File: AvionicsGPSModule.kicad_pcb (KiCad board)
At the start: 4 copper layers, 60 x 56.1 mm, 32 parts, among them P1 MC311D, Q1 AO3400A, U2 AP2112K-3.3, U3 L80-R, U4 RP2040, U6 W25Q128JVS, X1 ABM8-272-T3

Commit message: Connector Changes
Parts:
- moved R4 6.17 mm to (152.4, 93.6)
- moved R5 6.15 mm to (153.4, 93.6)
- moved R2 3.28 mm to (154.3, 80.0), turned to -90 degrees
- moved C17 2.51 mm to (157.5, 93.2)
- moved C19 2.51 mm to (158.5, 92.2)
- moved C1 2.49 mm to (156.5, 94.2)
- moved R3 1.99 mm to (151.4, 80.1), turned to -90 degrees
- moved P1 1.37 mm to (153.0, 75.8), turned to 180 degrees
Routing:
- net /DN: track 17.2 -> 0.58 mm
- net /DP: track 11.4 -> 0.58 mm
- net Net-(U4-USB_DM): track 8.39 -> 1.48 mm
- net Net-(U4-USB_DP): track 7.81 -> 1.21 mm
- net GND: track 92.9 -> 96.7 mm, vias 3 -> 6
- net Net-(P1-CC1): track 3.81 -> 1.44 mm
- net +5V: track 45.1 -> 44.9 mm, vias 4 -> 2

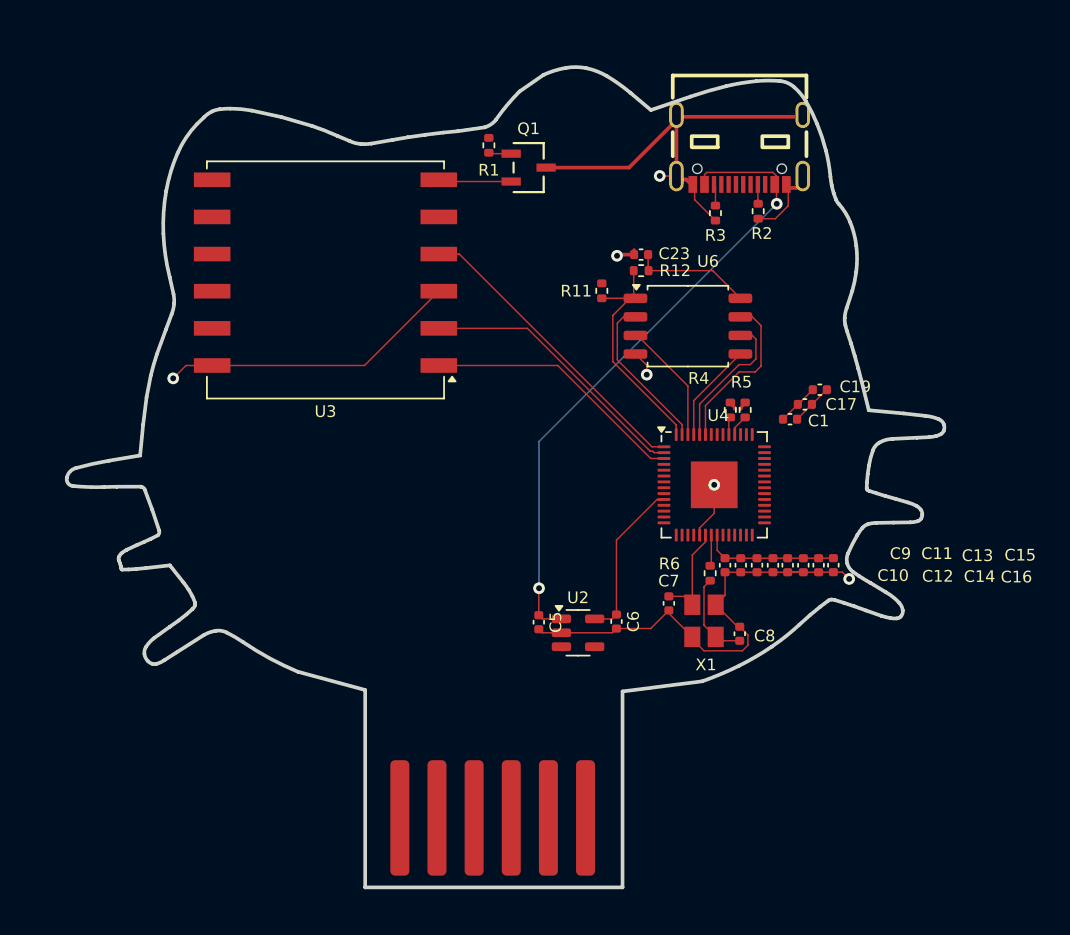
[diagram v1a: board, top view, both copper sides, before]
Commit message: Fix: Moved RP2040 capacitors
Fix: Corrected Design Rules for clearance and width

Fix: Correctly Annotated capacitors
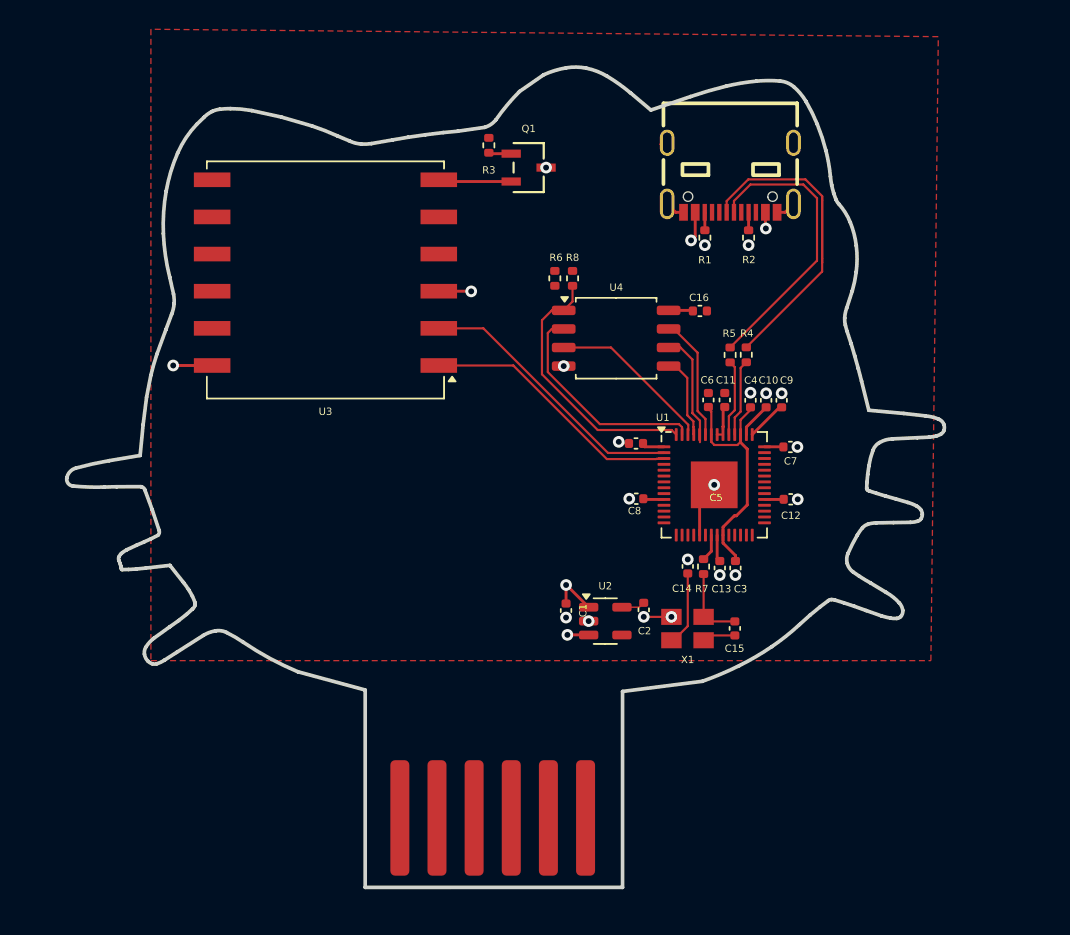
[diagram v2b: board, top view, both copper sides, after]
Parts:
- moved C3 13.5 mm to (152.8, 104.4), turned to -90 degrees
- moved C11 12.5 mm to (152.0, 92.9), turned to 90 degrees
- moved C8 11.7 mm to (145.9, 95.9), turned to 180 degrees
- moved C10 11.4 mm to (154.8, 92.9), turned to 90 degrees
- moved C9 11.3 mm to (155.9, 92.9), turned to 90 degrees
- moved C7 8.77 mm to (156.5, 96.1), turned to 0 degrees
- moved C13 7.77 mm to (151.7, 104.4)
- moved C5 7.59 mm to (146.0, 99.7), turned to 180 degrees
- moved C6 5.74 mm to (150.9, 92.9), turned to 90 degrees
- moved C16 5.57 mm to (150.3, 86.8), turned to 0 degrees
- moved U4 4.98 mm to (144.6, 88.7)
- moved C12 4.90 mm to (156.5, 99.7), turned to 0 degrees
- moved R8 4.72 mm to (141.6, 84.6), turned to -90 degrees
- moved R4 3.77 mm to (153.5, 89.8)
- moved R5 3.76 mm to (152.4, 89.8)
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- renumbered C5 to C1, C13 to C10, C14 to C11, C15 to C12, C16 to C13, C7 to C14, C8 to C15, C23 to C16, C6 to C2, C19 to C3, C17 to C4, C9 to C5, C1 to C6, C10 to C7, C11 to C8, C12 to C9, R3 to R1, R1 to R3, R5 to R4, R4 to R5, R11 to R6, R6 to R7, R12 to R8, U4 to U1, U6 to U4
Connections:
- C16 pad 1: +3V3 -> +3.3V
- R8 pad 1: +3V3 -> +3.3V
- U4 pad 8: +3V3 -> +3.3V
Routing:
- net GND: track 96.7 -> 16.9 mm, vias 6 -> 25
- net +5V: track 44.9 -> 7.89 mm, vias 2 -> 4
- net /DN: track 0.58 -> 25.4 mm
- net +3.3V: track 41.2 -> 17.5 mm
- net /DP: track 0.58 -> 20.0 mm
- net +1V1: track 2.85 -> 17.3 mm
- net +3V3: track 8.17 -> 0.00 mm
- net /QSPI_SD1: track 10.9 -> 15.1 mm
- net Net-(U1-USB_DP): track 1.21 -> 5.24 mm
- net Net-(U1-USB_DM): track 1.48 -> 5.27 mm
- net /QSPI_SD3: track 11.3 -> 7.95 mm
- net /QSPI_SD2: track 8.34 -> 11.1 mm
- net /QSPI_SS: track 16.2 -> 18.3 mm
- net /QSPI_SCLK: track 9.74 -> 7.84 mm
- net /XIN: track 6.97 -> 5.39 mm
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- added copper zone on F.Cu, net +3.3V

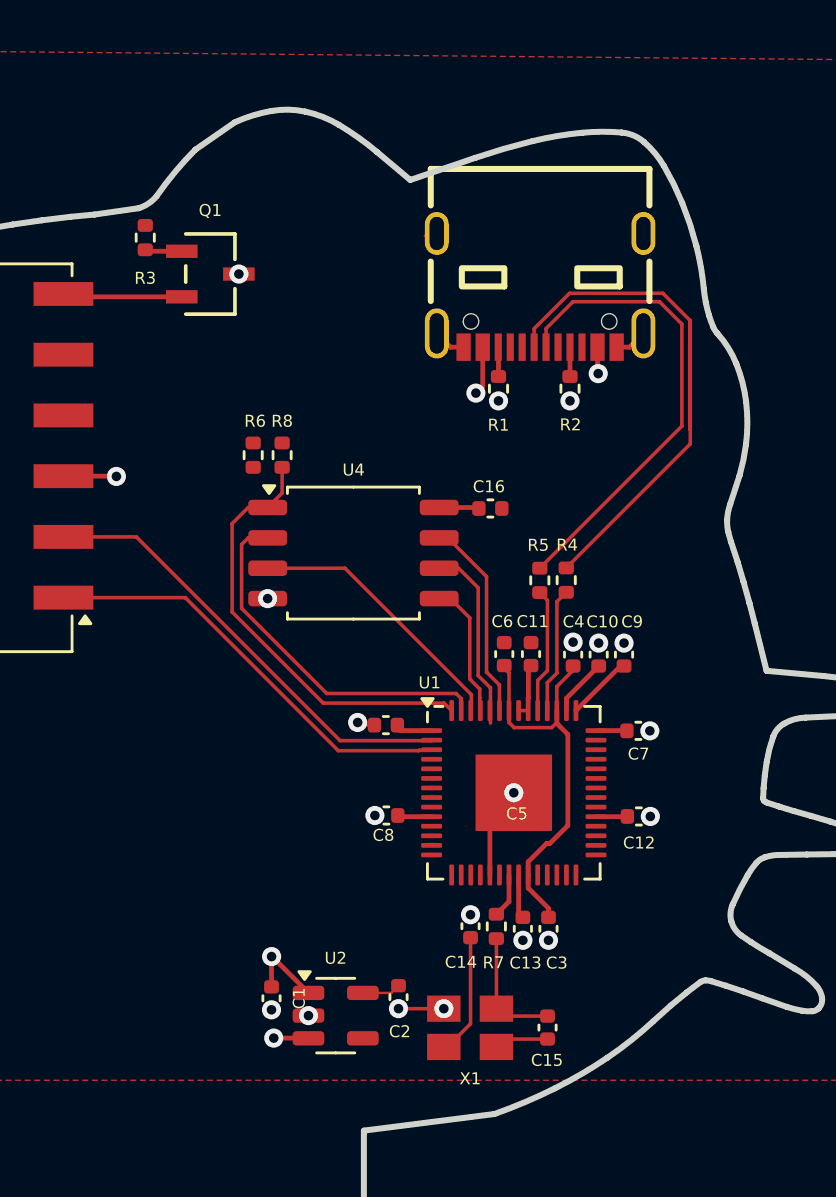
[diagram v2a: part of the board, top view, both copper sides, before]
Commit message: Fixed connector placement and GND vias
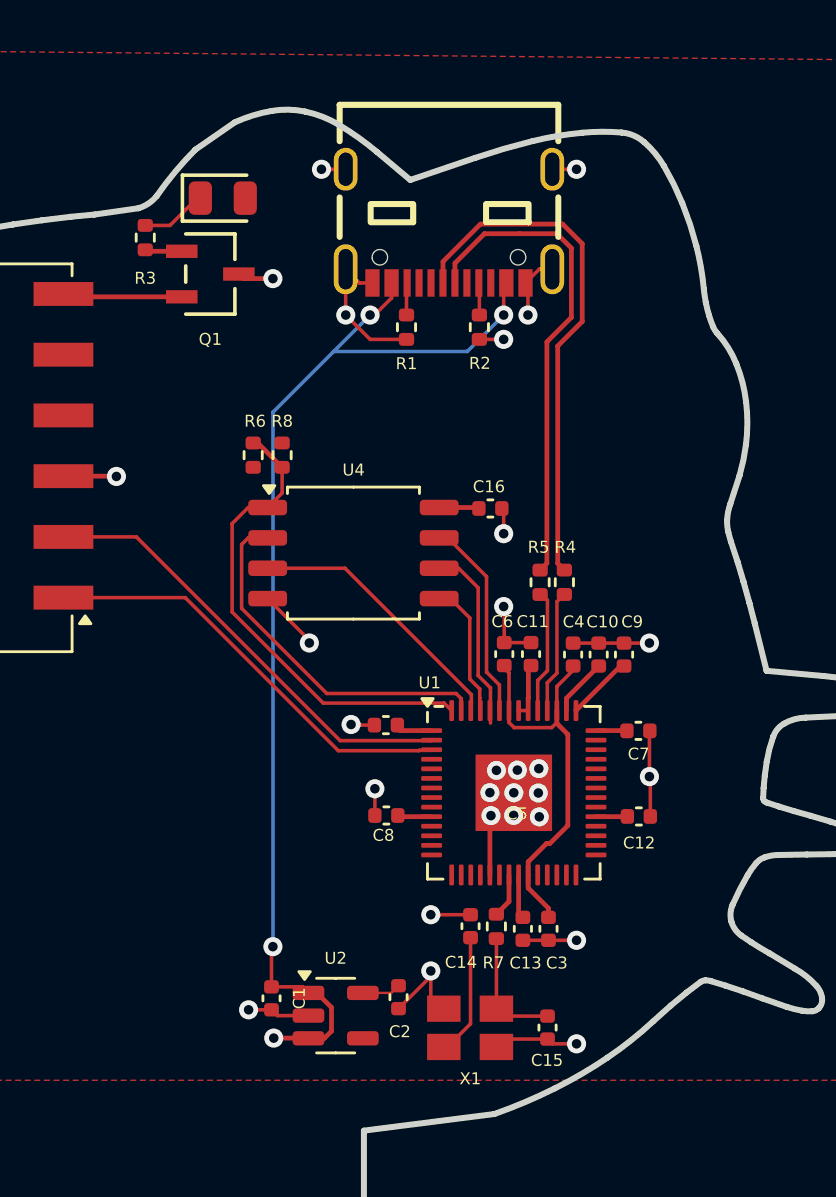
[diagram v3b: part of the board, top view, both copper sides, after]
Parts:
- added D2: Green, PCM_JLCPCB:D_0805, F.Cu at (139.1, 73.9)
- moved P1 4.66 mm to (148.6, 75.0)
- moved R1 4.63 mm to (146.8, 79.2)
- moved R2 4.58 mm to (149.9, 79.2)
- moved R4 0.12 mm to (153.4, 89.9)
- moved R5 0.08 mm to (152.4, 89.9)
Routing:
- net +5V: track 7.89 -> 47.2 mm
- net GND: track 16.9 -> 51.7 mm, vias 25 -> 29
- net /DN: track 25.4 -> 21.9 mm
- net Net-(D2-Pad1): track 0.00 -> 2.20 mm
- net /QSPI_SS: track 18.3 -> 19.9 mm

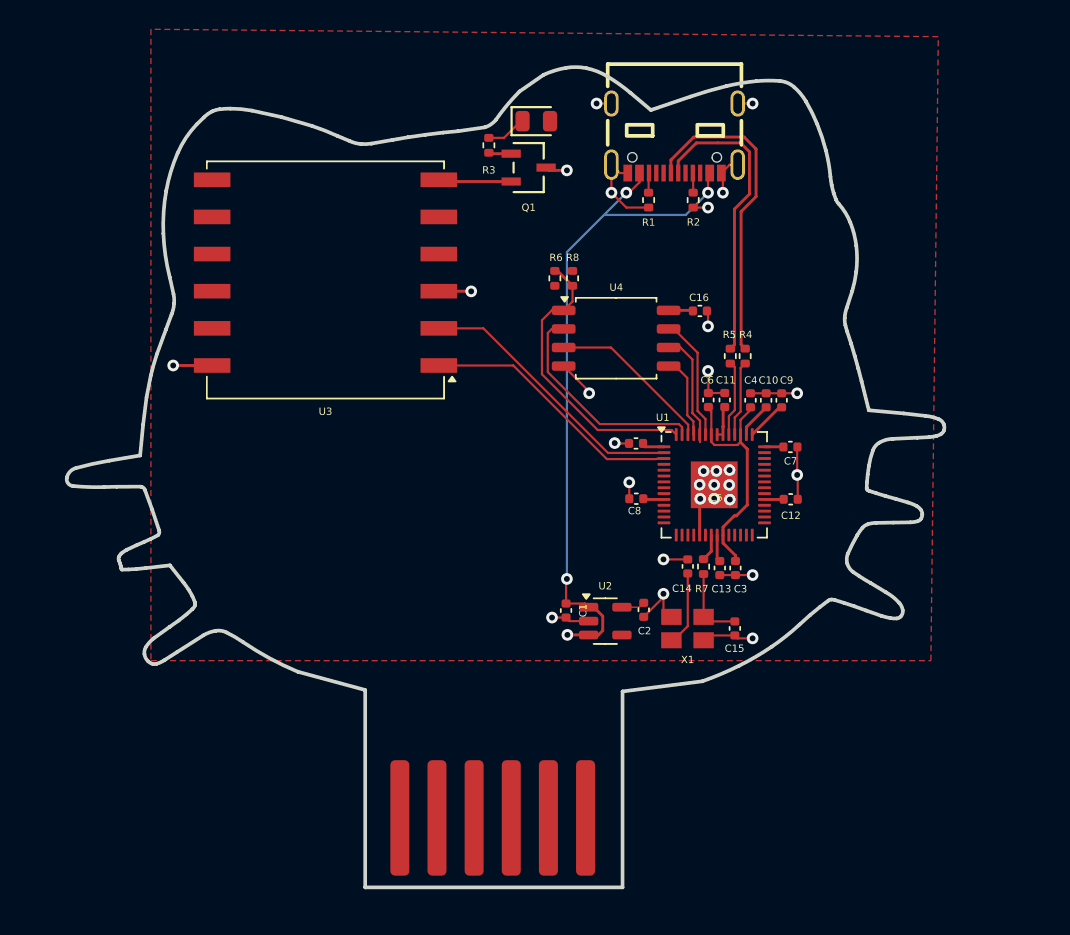
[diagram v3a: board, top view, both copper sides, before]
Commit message: Added JLC DRC requirements, and managed libraries for simpler forking
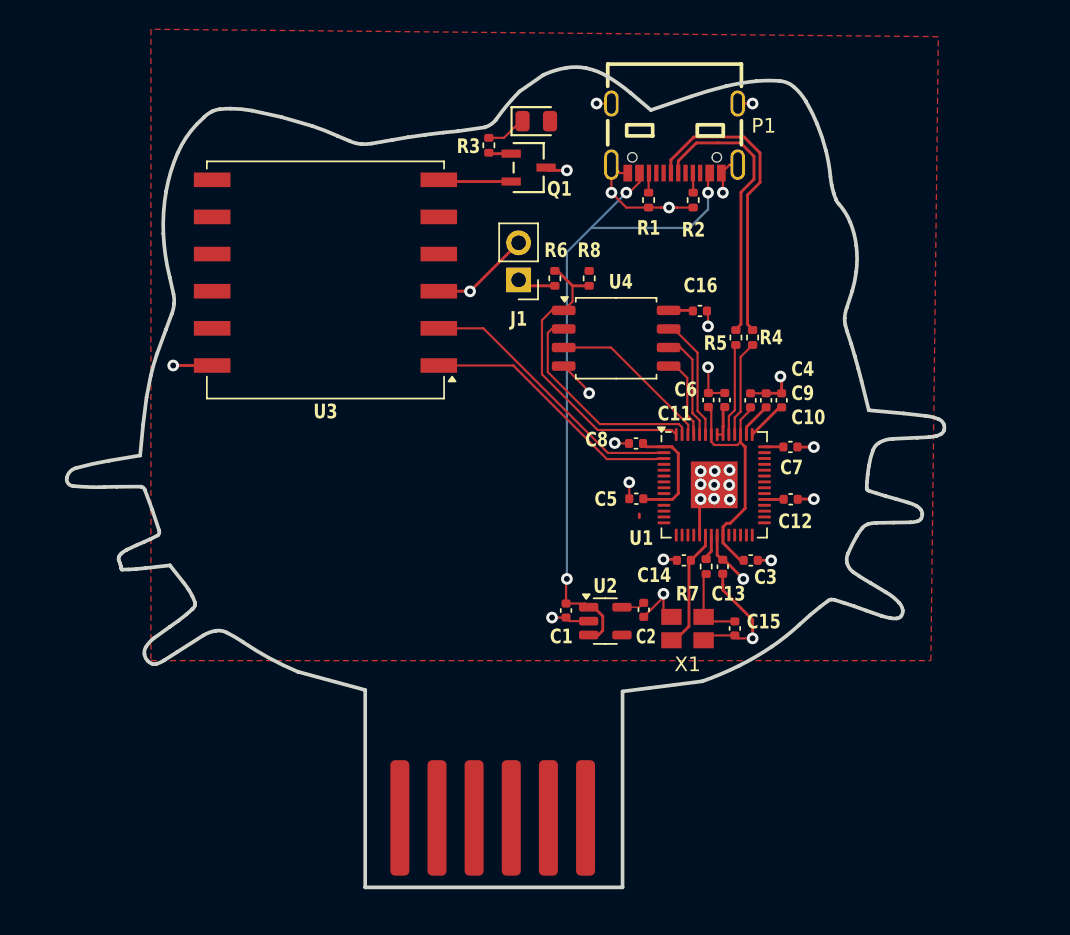
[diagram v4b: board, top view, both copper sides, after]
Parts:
- added J1: ~, Connector_PinHeader_2.54mm:PinHeader_1x02_P2.54mm_Vertical, F.Cu at (137.9, 84.7)
- P1: footprint MC311D:USB-C-SMD_MC-311D -> MC-311D:USB-C-SMD_MC-311D
- X1: footprint ABM8-272-T3:ABM8-272-T3_ABR -> ABM8_272_T3:ABM8-272-T3_ABR
- moved R4 1.37 mm to (153.9, 88.6)
- moved R5 1.33 mm to (152.8, 88.6)
- moved C3 1.17 mm to (153.8, 103.9), turned to 0 degrees
- moved R8 1.14 mm to (142.7, 84.6)
- moved C14 0.49 mm to (149.2, 103.9), turned to 180 degrees
- moved C13 0.22 mm to (151.9, 104.3)
- moved R7 0.18 mm to (150.7, 104.3)
- renumbered D2 to D1
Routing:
- net GND: track 51.7 -> 60.7 mm, vias 29 -> 30
- net +3.3V: track 17.5 -> 25.2 mm, vias 0 -> 1
- net /XIN: track 5.39 -> 8.45 mm
- net Net-(J1-USB_BOOT): track 0.00 -> 2.64 mm
- net Net-(U1-USB_DM): track 5.27 -> 6.63 mm
- net Net-(U1-USB_DP): track 5.24 -> 6.50 mm
- net /DP: track 20.5 -> 19.3 mm
- net /QSPI_SS: track 19.9 -> 21.0 mm
- net /DN: track 21.9 -> 21.0 mm
- net /QSPI_SCLK: track 7.84 -> 7.31 mm
- net +5V: track 47.2 -> 47.6 mm, vias 4 -> 3

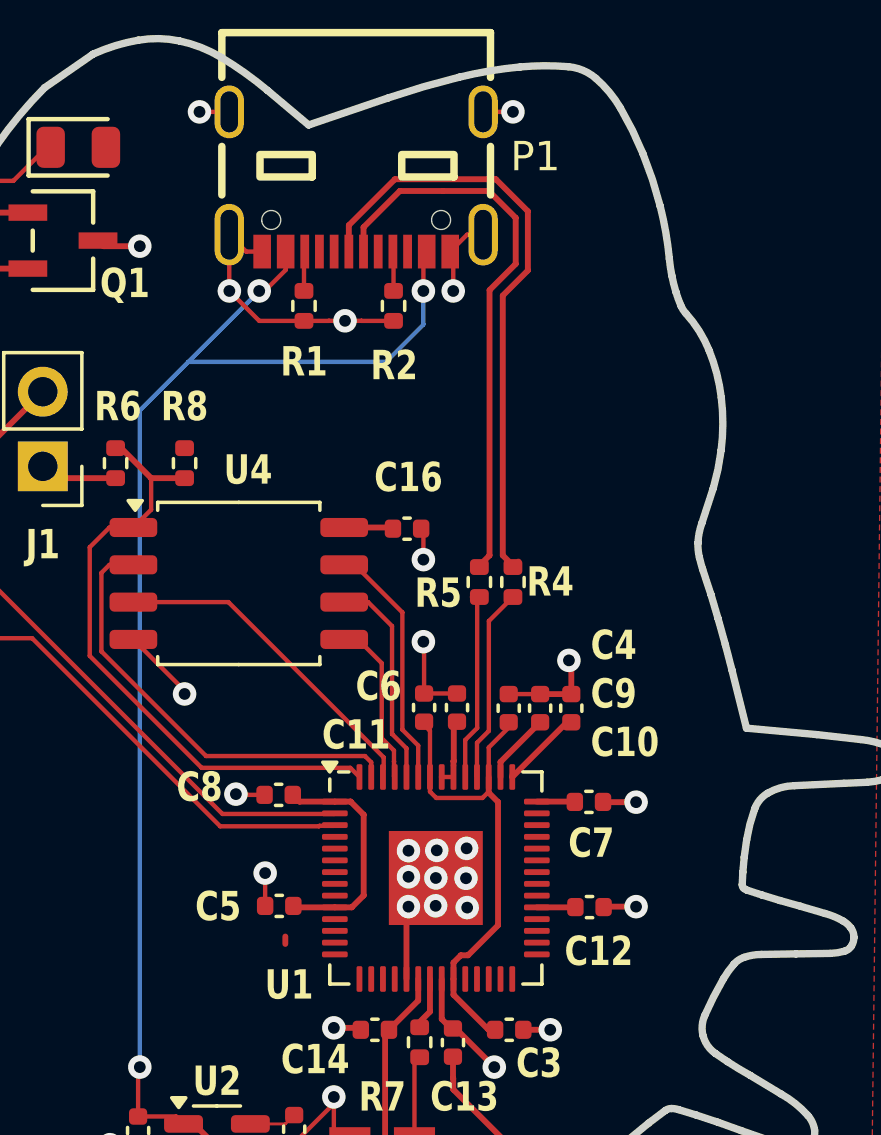
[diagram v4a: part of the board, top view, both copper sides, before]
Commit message: Fixed Differential Pair Wiring
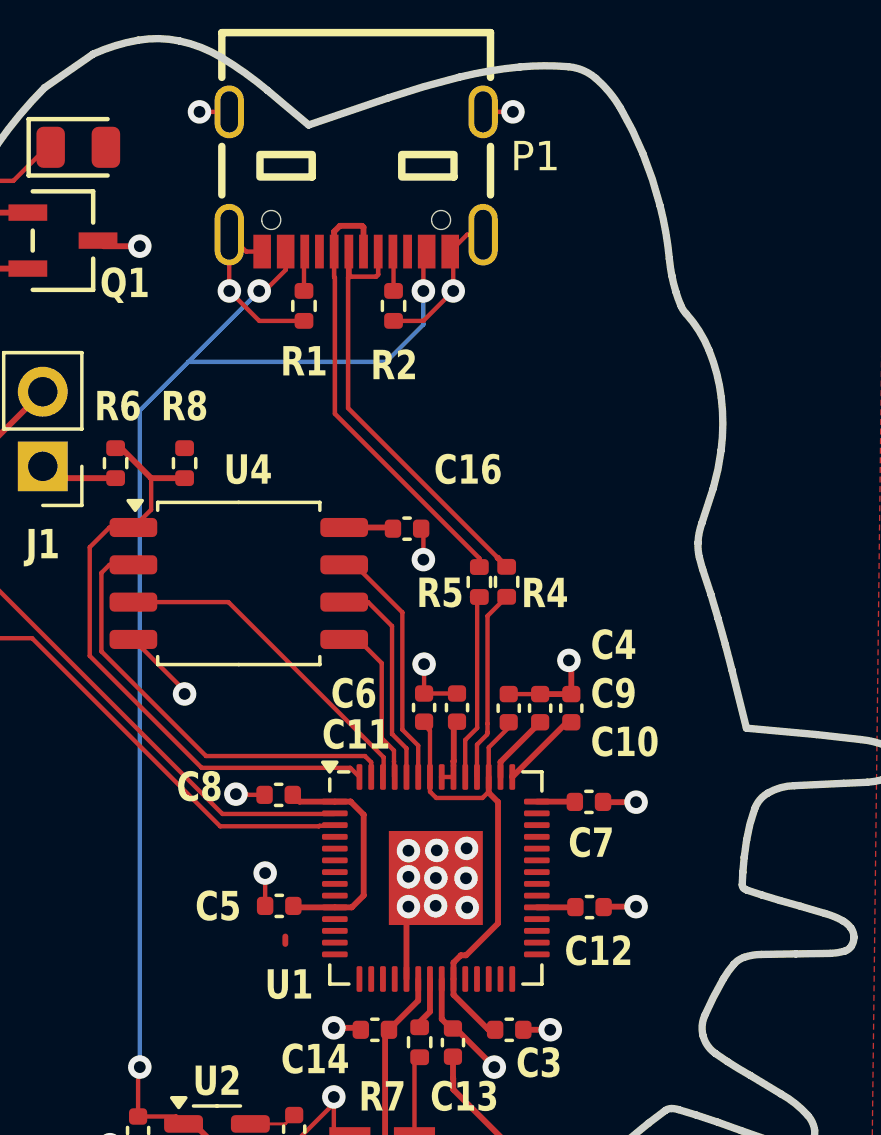
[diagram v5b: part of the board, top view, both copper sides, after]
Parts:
- moved R4 0.21 mm to (153.7, 88.6)
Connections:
- P1 pad B6: /USB_DP -> /DP
- P1 pad B7: /USB_DM -> /DN
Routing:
- net /DN: track 21.0 -> 15.6 mm
- net /DP: track 19.3 -> 15.4 mm
- net GND: track 60.7 -> 59.4 mm, vias 30 -> 29

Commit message: minor changes
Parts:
- moved R4 0.17 mm to (153.9, 88.7)
- moved C11 0.05 mm to (152.0, 92.9)
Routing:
- net +3.3V: track 25.2 -> 31.9 mm, vias 1 -> 3
- net +1V1: track 17.5 -> 18.7 mm
